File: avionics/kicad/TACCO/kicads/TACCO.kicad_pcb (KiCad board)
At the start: 6 copper layers, 55 x 35 mm, 170 parts, among them X2Y-CAN 4.7nF X2Y, X2Y-RS485 4.7nF X2Y

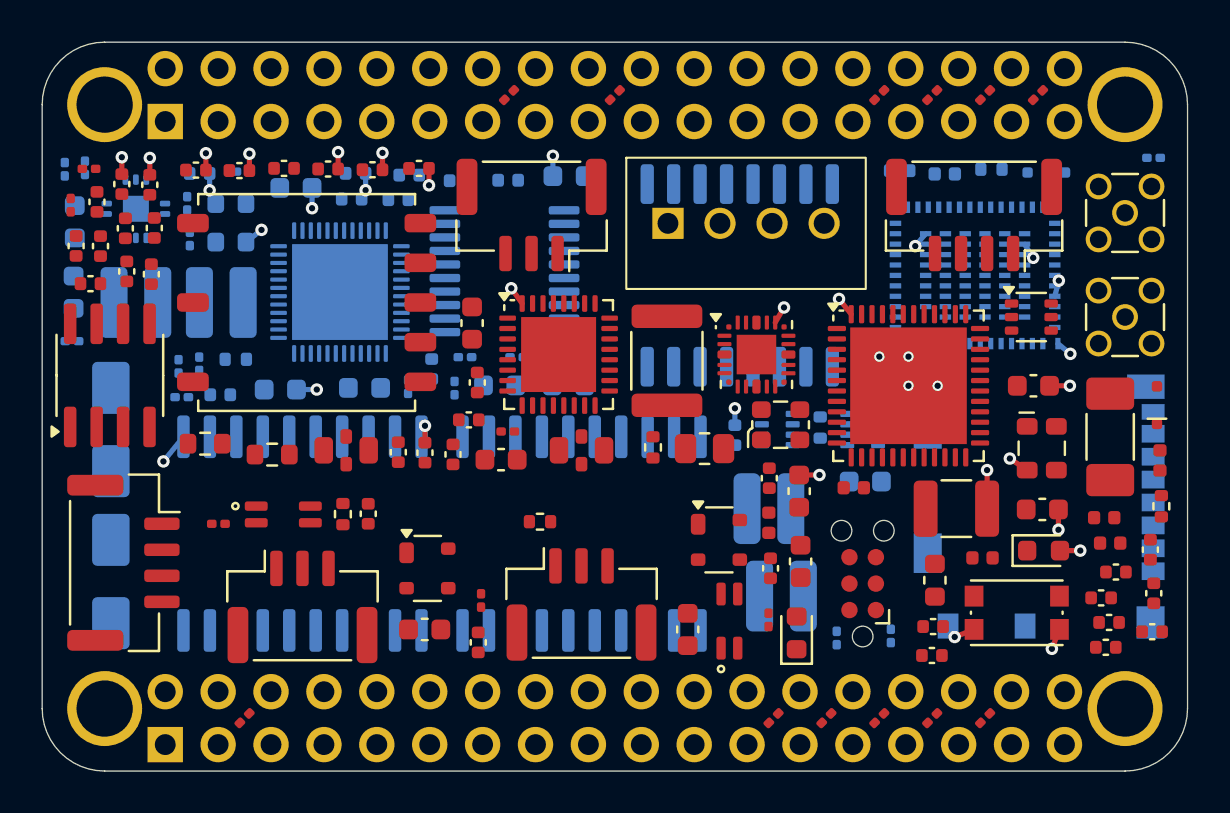
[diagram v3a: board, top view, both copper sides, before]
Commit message: TACCO: import freerouting phase-1 pass (logic nets, band closed)
Imports the first Specctra session (1502 segments, 151 vias) into the
prepared Rev S3 board and fills the inner GND/+3V3 planes.  DRC: 0
errors, 0 parity issues, 216 connections still unrouted (isolation-band
nets are deferred to phase 2; the remainder continue in a second run
started from this state).

Co-Authored-By: Claude Fable 5.1 <noreply@anthropic.com>
Claude-Session: https://claude.ai/code/session_01YLwDy53g1VCBzNBwW4moUC
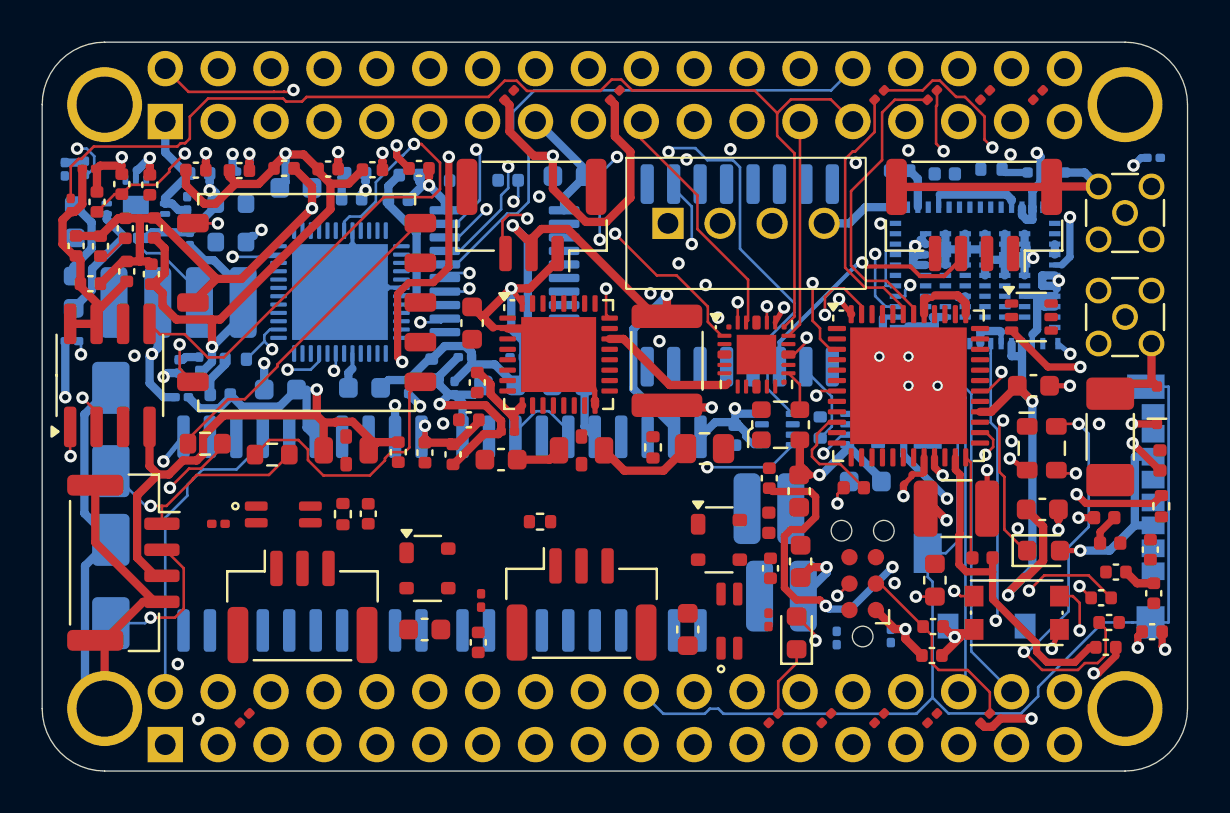
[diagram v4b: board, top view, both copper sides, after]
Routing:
- net GND: track 24.5 -> 239.9 mm
- net PGND: track 0.00 -> 117.0 mm
- net +1V8_RF: track 0.00 -> 103.2 mm, vias 0 -> 7
- net +5V: track 0.00 -> 95.9 mm, vias 0 -> 6
- net +3V3_RF: track 0.00 -> 91.2 mm, vias 0 -> 6
- net SPI0_B_MISO: track 0.00 -> 68.6 mm, vias 0 -> 3
- net +3V3: track 4.29 -> 69.6 mm, vias 4 -> 5
- net MLRS_TX_F: track 0.00 -> 63.2 mm, vias 0 -> 4
- net SD_CD: track 0.00 -> 56.3 mm
- net MDIO0: track 0.00 -> 55.6 mm, vias 0 -> 3
- net RMII2_RXD0: track 0.00 -> 54.2 mm
- net SPI0_B_CS_FLASH: track 0.00 -> 52.4 mm, vias 0 -> 1
- net +5V_IN: track 0.00 -> 48.2 mm, vias 0 -> 3
- net FB_3V3: track 0.00 -> 46.8 mm, vias 0 -> 3
- net +3V3_PB2: track 0.00 -> 45.1 mm, vias 0 -> 1
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
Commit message: TACCO: split plane-fed rails into a 0.2 mm PLANE netclass for routing
After two freerouting passes ~70 of the ~160 open non-isolation
connections were GND/+3V3/+3V3_RF/+1V8_RF pins at 0.5 mm-pitch QFN pads
ringed by 0201 bypasses: the POWER class forced 0.4 mm stubs the escape
geometry cannot admit.  Those rails are plane-fed (In1 GND, In4 +3V3), so
their routing-layer copper is only pad-to-via stubs; give them a PLANE
class at 0.2 mm and keep POWER (+5V*, PGND) at 0.4 mm.  Board carries the
second phase-1 import (1967 segments, 155 vias; DRC 0 errors, 198 open).
finish_tacco_pcb.py docstring records the freerouting pass-cap and
normalization-dialog behaviour.

Co-Authored-By: Claude Fable 5.1 <noreply@anthropic.com>
Claude-Session: https://claude.ai/code/session_01YLwDy53g1VCBzNBwW4moUC
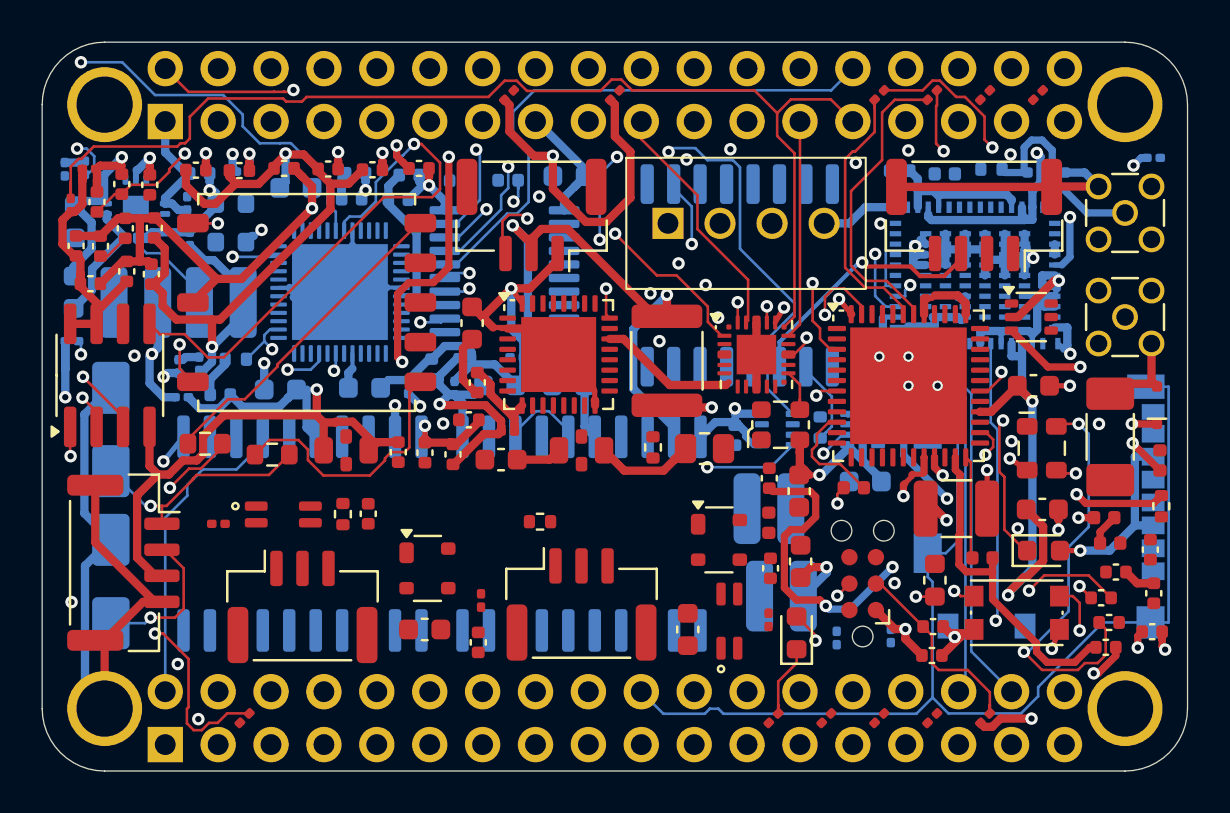
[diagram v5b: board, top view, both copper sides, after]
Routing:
- net SPI0_B_MISO: track 68.6 -> 102.6 mm, vias 3 -> 4
- net GND: track 239.9 -> 269.7 mm
- net FLASH_WP_N: track 0.00 -> 28.0 mm, vias 0 -> 3
- net RADIO_ANT_F: track 1.29 -> 9.74 mm
- net +1V8_RF: track 103.2 -> 108.6 mm
- net +5V: track 95.9 -> 100.4 mm
- net +3V3: track 69.6 -> 73.5 mm
- net RMII2_RXD0: track 54.2 -> 54.9 mm
- net MLRS_RST: track 9.43 -> 10.1 mm

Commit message: TACCO: clear the P2 inter-row channel; keep owner GUI project settings
The P2 header positions under the isolation band (P2-3..P2-24: MCAN0,
MDIO0, TPM/1553/PHY control) can only leave along the gap between the two
socket rows, with vias at the 2x2 pin-cell centres: the band closes every
layer to the north and the board edge closes the south.  Six 0201 parts
parked in P2 rail cells blocked that channel and left 15 nets unroutable
in the 2026-09-30 freerouting passes.  Rail cells are now P1-row only;
all 170 parts still place, DRC 0 errors / 0 parity issues after the
prepare step (9 QFN thermal vias, 32 plane fan-out vias).

gen_tacco_pcb.py also stops discarding the settings the owner saves from
the KiCad GUI (ERC pin map, BOM presets, schematic options): SaveBoard()
rewrites TACCO.kicad_pro from a host-less BOARD, so the prior file is
merged back in its own key order and only the generator-owned netclass
and rule keys change.

The board is placed and prepared, not yet routed; routing follows.

Co-Authored-By: Claude Opus 5.5 <noreply@anthropic.com>
Claude-Session: https://claude.ai/code/session_01YLwDy53g1VCBzNBwW4moUC
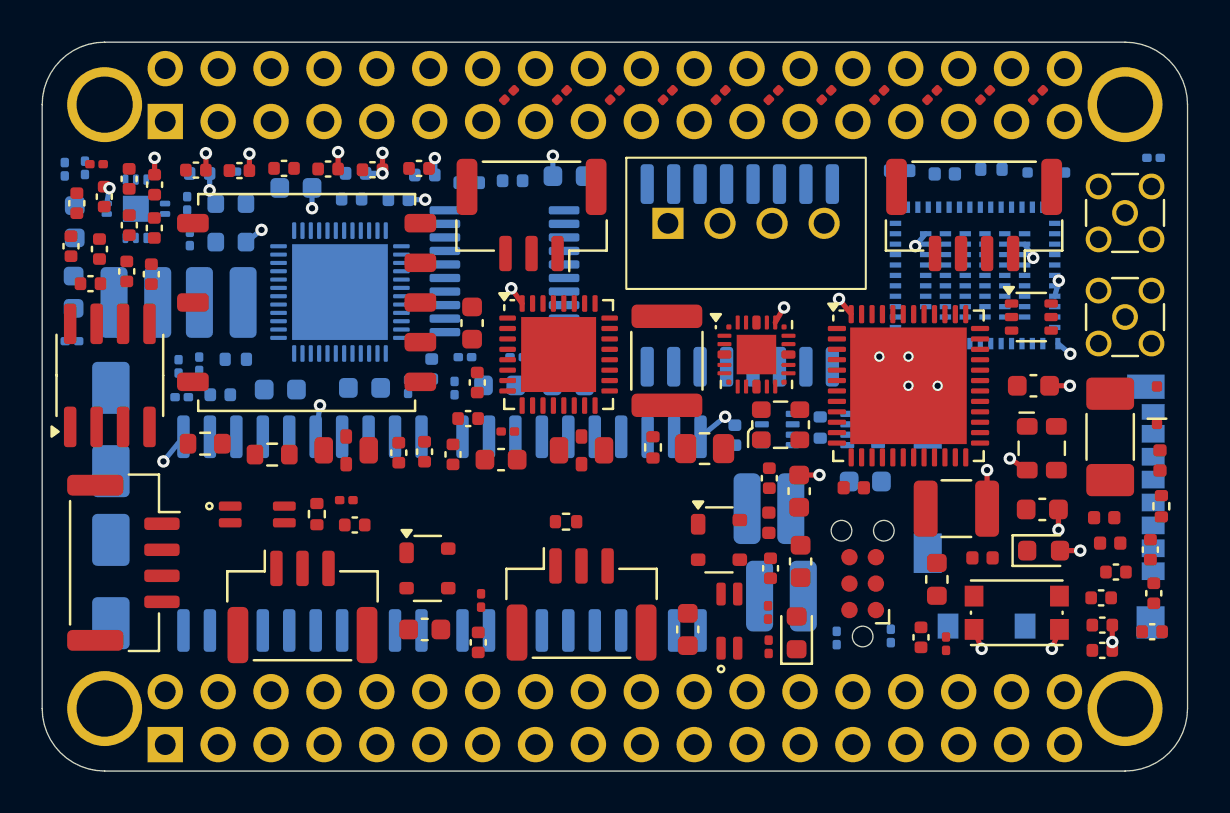
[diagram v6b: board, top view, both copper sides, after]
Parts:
- C-BST18, C-MLRS-SH2: moved to F.Cu
- C-MLRS-VRPA, R-AD0: moved to B.Cu
- moved R-AD0 40.3 mm to (161.7, 103.8)
- moved C-MLRS-TX0 34.0 mm to (139.4, 107.2), turned to 90 degrees
- moved C-MLRS-TCXO 32.3 mm to (141.5, 105.6)
- moved C-BST18 31.2 mm to (163.2, 116.1), turned to 90 degrees
- moved R-MLRS-LEDR 30.0 mm to (153.6, 90.0)
- moved R-MLRS-RST 30.0 mm to (168.8, 90.0)
- moved R-FB18H 29.9 mm to (161.2, 90.0)
- moved R-FB18L 29.9 mm to (158.7, 90.0)
- moved R-MLRS-BOOT0 29.9 mm to (163.7, 90.0)
- moved R-FLASH-WP 25.4 mm to (155.9, 116.5), turned to 90 degrees
- moved R-MLRS-SWDIO 20.3 mm to (148.5, 90.0)
- moved C-MLRS-VFB 18.8 mm to (126.4, 94.3), turned to 90 degrees
- moved C-MLRS-VRPA 13.4 mm to (141.5, 94.2), turned to 0 degrees
- moved R-MLRS-SWCLK 12.7 mm to (151.0, 90.0)
- moved C-MLRS-SH2 12.5 mm to (155.9, 114.9)
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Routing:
- net GND: track 269.7 -> 26.6 mm, vias 31 -> 32
- net PGND: track 117.4 -> 0.00 mm
- net +1V8_RF: track 108.6 -> 0.00 mm, vias 7 -> 0
- net SPI0_B_MISO: track 102.6 -> 0.00 mm, vias 4 -> 0
- net +5V: track 100.4 -> 0.00 mm, vias 6 -> 0
- net +3V3_RF: track 91.2 -> 0.00 mm, vias 6 -> 0
- net +3V3: track 73.5 -> 4.29 mm, vias 5 -> 4
- net MLRS_TX_F: track 63.6 -> 0.00 mm, vias 4 -> 0
- net SD_CD: track 56.3 -> 0.00 mm
- net MDIO0: track 55.6 -> 0.00 mm, vias 3 -> 0
- net RMII2_RXD0: track 54.9 -> 0.00 mm
- net SPI0_B_CS_FLASH: track 52.4 -> 0.00 mm, vias 1 -> 0
- net +5V_IN: track 48.3 -> 0.00 mm, vias 3 -> 0
- net FB_3V3: track 46.8 -> 0.00 mm, vias 3 -> 0
- net +3V3_PB2: track 45.1 -> 0.00 mm, vias 1 -> 0
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
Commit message: TACCO: make placement deterministic; add what-if hook for layout experiments
The placer walked a Python set of net names to pick each part's anchor,
so placement followed PYTHONHASHSEED and moved ~23 parts between two runs
of the same generator.  The walk is now sorted, and two consecutive runs
place all 170 parts identically.  The committed board is regenerated from
that deterministic placement (DRC 0 errors, 0 parity issues; 9 thermal
and 34 plane fan-out vias).

TACCO_WHATIF=<json> lets the connector / rail-socket optimization runs
override fixed positions, footprints and rail cells and write to a
scratch directory, so every experiment is a regenerated board rather
than a hand edit.  Unset, the generator behaves exactly as before.

Co-Authored-By: Claude Opus 5.5 <noreply@anthropic.com>
Claude-Session: https://claude.ai/code/session_01YLwDy53g1VCBzNBwW4moUC
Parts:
- C-BST18: moved to B.Cu
- C-MLRS-VRPA: moved to F.Cu
- moved R-FLASH-WP 39.8 mm to (122.2, 95.3)
- moved C-MLRS-TCXO 34.3 mm to (174.2, 115.7)
- moved C-MLRS-TX0 34.0 mm to (172.0, 116.7), turned to 0 degrees
- moved C-BST18 31.0 mm to (141.3, 94.2), turned to 0 degrees
- moved R-MLRS-LEDG 26.5 mm to (155.8, 116.5), turned to 90 degrees
- moved C-MLRS-VFB 18.8 mm to (141.5, 105.6), turned to 0 degrees
- moved C-MLRS-VRPA 13.4 mm to (138.1, 107.2), turned to 90 degrees
- moved C-MLRS-RXN 10.6 mm to (163.7, 116.9)
- moved C-MLRS-SH1 10.0 mm to (174.4, 116.8), turned to 0 degrees
- moved C-MLRS-RST 8.13 mm to (163.8, 115.6)
- moved C-CAN4 6.25 mm to (129.5, 110.6)
- moved C-PHY-A2 4.30 mm to (126.2, 94.3)
- moved C-PHY-CTD1 3.30 mm to (124.8, 94.3)
- moved R-MLRS-SWCLK 2.54 mm to (153.6, 90.0)
- moved R-MLRS-LEDR 2.54 mm to (156.1, 90.0)
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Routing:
- net GND: track 26.6 -> 27.5 mm, vias 32 -> 34

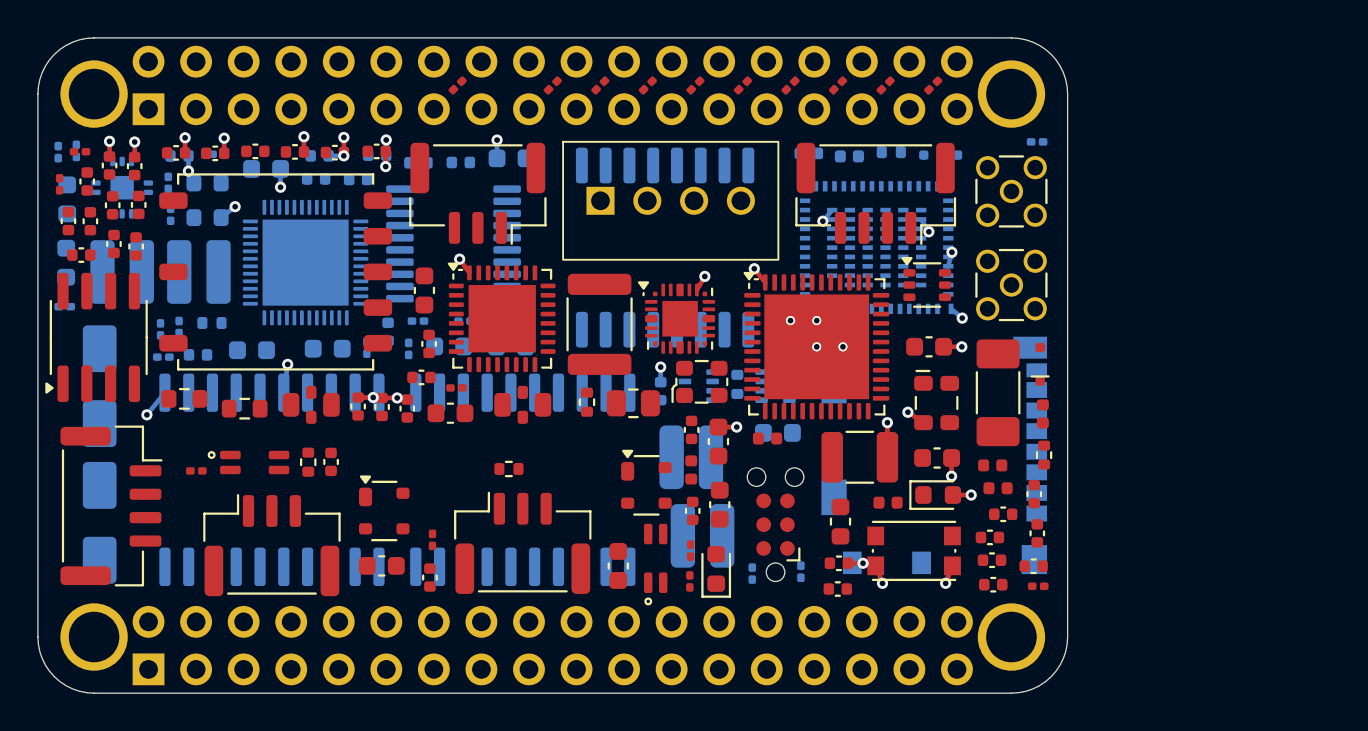
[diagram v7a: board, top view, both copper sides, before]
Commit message: TACCO: SSM-DV-LC rails, redrawn isolation band, single TPS63031 inductor (WIP placement)
- PB2 rails -> Samtec SSM-118-L-DV-LC SMT sockets (footprint from samtec_ssm_footprint.pdf
  Rev D Fig. 4, -LC clip holes as through-board anchors); WBS R3 owner decision 2026-10-05.
- Isolation band redrawn: transceivers top face, bus connectors at the bottom edge; band on
  F.Cu + inner layers only, B.Cu beneath it limited to B-routable parts.
- TPS63031 fix: one inductor across L1-L2 per tps63031.pdf (L-RF2 removed).
- Placer: children after their anchor parent; THT/NPTH holes checked against the opposite
  face's copper.
- Docs: WBS, TACCO.md §13a, CONCEPTS.md, PB2 learning docs corrected for 4.80 mm rails.

Placement is not yet closed: the committed board still has parts parked off-outline; routing
and fab outputs follow once a full placement is found.

Co-Authored-By: Claude Opus 5.5 <noreply@anthropic.com>
Claude-Session: https://claude.ai/code/session_01YLwDy53g1VCBzNBwW4moUC
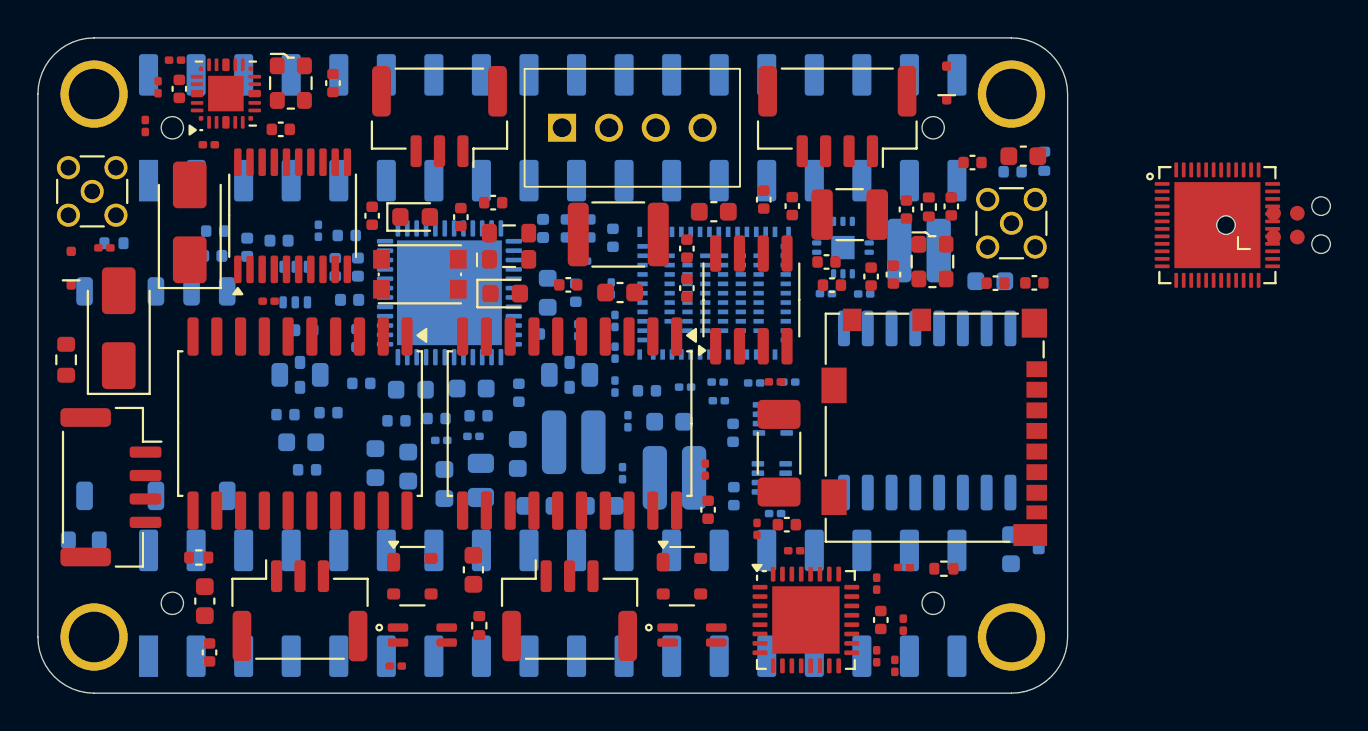
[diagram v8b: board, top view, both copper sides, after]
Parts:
- removed L-RF2: 2.2uH 3A, Inductor_SMD:L_Wuerth_MAPI-3015
- 1553-XCVR, C-1553A, C-1553B, C-1553C, C-1553D, C-25M, C-50M, C-BST18, C-CAN1, C-PLD1, C-RF-IN2, C-TPM2, C-TPM3, CAN-TR, D-ANT-RADIO, J-SD, L-ANT-SER, R-AD0, R-RBIAS, RS485, SD-WB, TVS-1553N, TVS-1553P, X-50M: moved to F.Cu
- 1553-XFM, C-1V8RF-HF, C-1V8RF-O1, C-1V8RF-O2, C-ANT-SH2, C-MLRS-BULK, C-MLRS-RST, C-MLRS-RX1, C-MLRS-RXN, C-MLRS-RXP, C-MLRS-SMPS, C-MLRS-TX1, C-MLRS-TX2, C-MLRS-VBAT, C-MLRS-VDD1, C-MLRS-VDD2, C-MLRS-VDDA1, C-MLRS-VDDA2, C-MLRS-VDDPA1, C-MLRS-VDDPA2, C-MLRS-VDDRF, C-MLRS-VFB, C-MLRS-VRPA, C-ZB-VIO, FB-MLRS-1, FB-MLRS-2, L-MLRS-PA, L-MLRS-RX2, L-MLRS-SER, L-MLRS-SMPS, L-MLRS-TX1, L-MLRS-TX2, MLRS-MCU, R-1553P, R-MLRS-BOOT0, R-MLRS-LEDG, R-MLRS-LEDR, R-MLRS-RST, R-MLRS-SWCLK, R-MLRS-SWDIO, R-PGND, RFSW-MLRS, X2Y-CAN, X2Y-RS485: moved to B.Cu
- L-RF1: value 2.2uH 3A -> 1.5uH
- PB2-P1: footprint Serenity-Custom:PocketBeagle2_2x18_P1_Socket -> Serenity-Custom:PocketBeagle2_2x18_P1_SSM-DV-LC
- PB2-P2: footprint Serenity-Custom:PocketBeagle2_2x18_P2_Socket -> Serenity-Custom:PocketBeagle2_2x18_P2_SSM-DV-LC
- moved C-MLRS-SH1 53.1 mm to (124.6, 98.7)
- moved D-ANT-MLRS 52.0 mm to (122.8, 99.8)
- moved L-MLRS-SER 51.0 mm to (125.1, 98.5), turned to 0 degrees
- moved J-ANT-MLRS 49.4 mm to (123.9, 95.7)
- moved 1553-XCVR 48.7 mm to (184.0, 97.5)
- moved C-TPM4 48.4 mm to (165.8, 116.6), turned to 90 degrees
- moved C-TPM1 48.3 mm to (166.0, 118.6)
- moved R-1553IRQ 45.3 mm to (174.8, 94.1), turned to 90 degrees
- moved L-MLRS-TX2 43.7 mm to (130.3, 99.1)
- moved L-RF1 42.6 mm to (168.1, 98.9)
- moved C-PHY-CRD1 41.9 mm to (166.7, 100.1)
- moved L-MLRS-RX2 41.8 mm to (133.9, 98.3), turned to 0 degrees
- moved C-PHY-CRD2 41.8 mm to (165.5, 100.2)
- moved L-MLRS-TX1 41.5 mm to (132.2, 98.7), turned to 90 degrees
- moved C-PHY-CTD2 39.7 mm to (163.1, 99.5), turned to 0 degrees
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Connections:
- L-RF1 pad 2: +5V -> RF_SW2
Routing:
- net GND: track 27.5 -> 0.00 mm, vias 34 -> 0
- net +3V3: track 4.29 -> 0.00 mm, vias 4 -> 0
